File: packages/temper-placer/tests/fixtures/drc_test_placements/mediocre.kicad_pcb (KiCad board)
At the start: 2 copper layers, 50 x 30 mm, 4 parts, among them U1 LM358

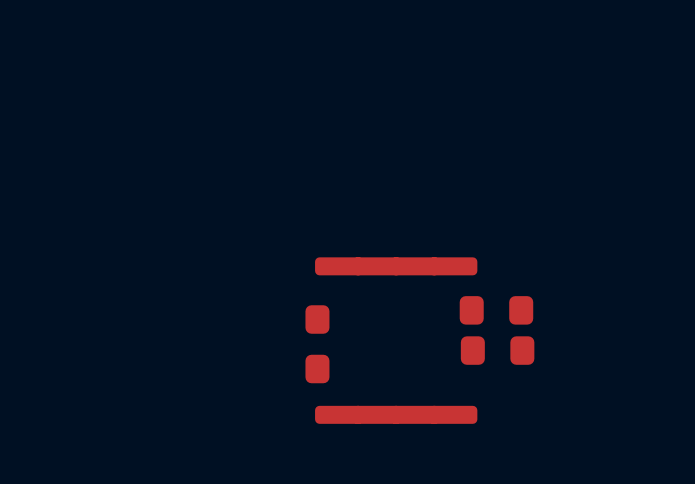
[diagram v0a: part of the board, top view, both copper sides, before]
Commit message: feat(placer): NSGA-II, Crawler, NetCentroidLoss, and structural refinements
- Implemented NSGA-II multi-objective optimization
- Added PcbCrawler for GitHub data collection
- Implemented NetCentroidAttractionLoss
- Unified optimization pipeline with explicit phases
- Fixed ruff linting errors and optimized imports
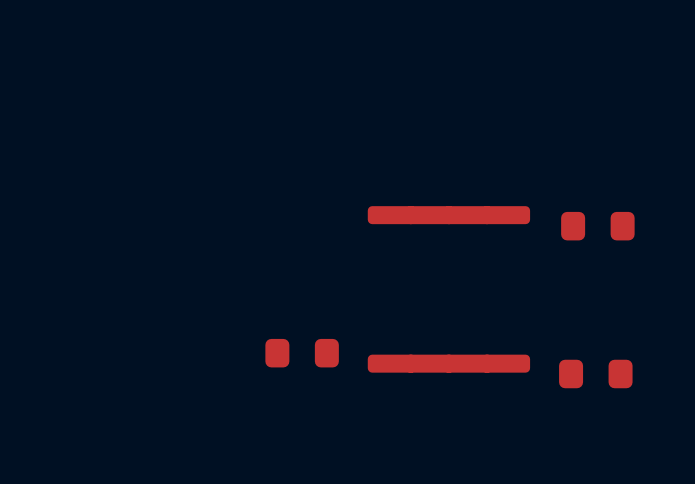
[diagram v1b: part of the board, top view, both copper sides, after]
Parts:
- moved C1 4.39 mm to (209.1, 149.6), turned to 180 degrees
- moved R2 3.37 mm to (209.0, 154.5)
- moved U1 2.45 mm to (204.1, 151.7)
- moved R1 0.59 mm to (199.2, 153.8), turned to 180 degrees
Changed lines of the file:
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@@
   (net 4 "SIG2")
   (footprint "Resistor_SMD:R_0603_1608Metric" (layer "F.Cu")
-    (at 199.748772873673 153.51630763178667 90.0)
+    (at 199.2375696681596 153.81366396913302 180.0)
     (property "Reference" "R1")
     (property "Value" "10k")
@@
   )
   (footprint "Resistor_SMD:R_0603_1608Metric" (layer "F.Cu")
-    (at 205.7534685396509 153.72662510139173 0.0)
+    (at 209.0270611652515 154.5077808807559 0.0)
     (property "Reference" "R2")
     (property "Value" "4.7k")
@@
   )
   (footprint "Capacitor_SMD:C_0603_1608Metric" (layer "F.Cu")
-    (at 205.71572434426218 152.38670351602337 0.0)
+    (at 209.0957264059502 149.57992738646345 180.0)
     (property "Reference" "C1")
     (property "Value" "100nF")
@@
   )
   (footprint "Package_SO:SOIC-8_3.9x4.9mm_P1.27mm" (layer "F.Cu")
-    (at 202.37346147158888 153.3943308817871 90.0)
+    (at 204.1311600303306 151.6876553482217 90.0)
     (property "Reference" "U1")
     (property "Value" "LM358")

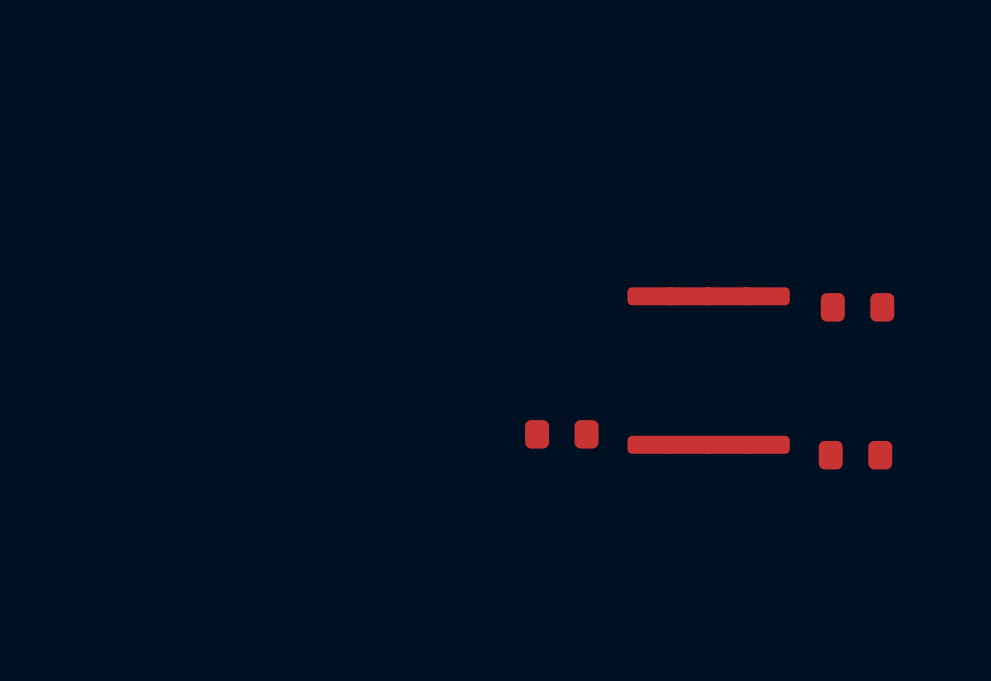
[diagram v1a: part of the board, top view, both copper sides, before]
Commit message: feat(placer): vectorize GroundCrossingLoss and add star-ground awareness
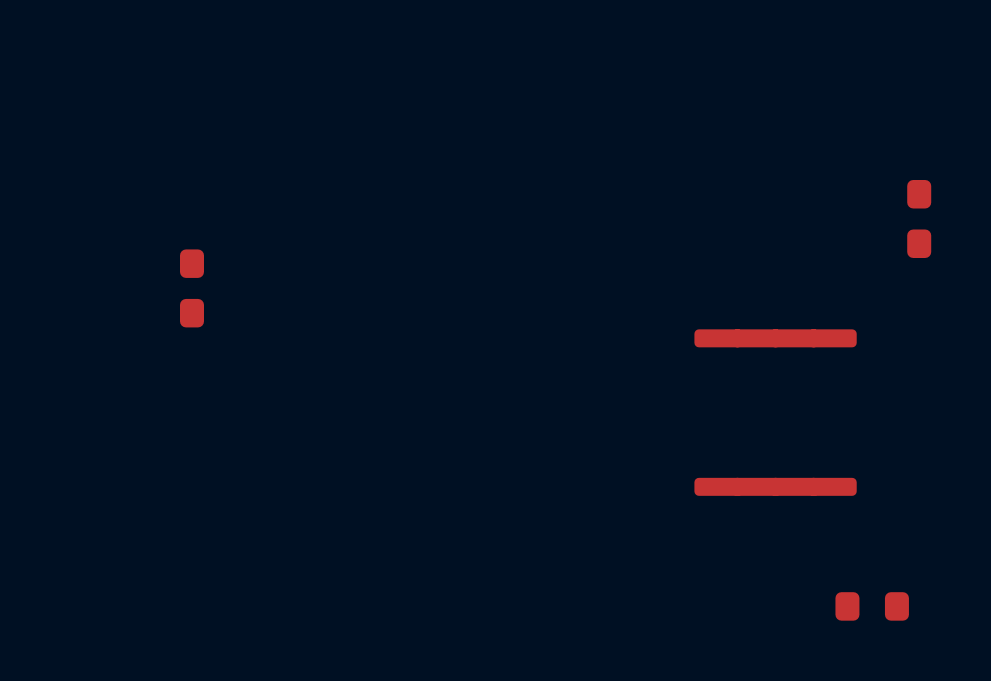
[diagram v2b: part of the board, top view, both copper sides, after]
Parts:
- moved R1 13.3 mm to (186.9, 148.9), turned to 90 degrees
- moved R2 5.07 mm to (209.6, 159.5), turned to 180 degrees
- moved C1 3.59 mm to (211.2, 146.6), turned to 270 degrees
- moved U1 2.63 mm to (206.4, 153.1)
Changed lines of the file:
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@@
   (net 4 "SIG2")
   (footprint "Resistor_SMD:R_0603_1608Metric" (layer "F.Cu")
-    (at 199.2375696681596 153.81366396913302 180.0)
+    (at 186.91073359716347 148.9497742597683 90.0)
     (property "Reference" "R1")
     (property "Value" "10k")
@@
   )
   (footprint "Resistor_SMD:R_0603_1608Metric" (layer "F.Cu")
-    (at 209.0270611652515 154.5077808807559 0.0)
+    (at 209.58405890750464 159.54938949343563 180.0)
     (property "Reference" "R2")
     (property "Value" "4.7k")
@@
   )
   (footprint "Capacitor_SMD:C_0603_1608Metric" (layer "F.Cu")
-    (at 209.0957264059502 149.57992738646345 180.0)
+    (at 211.1511315029556 146.63530564857916 270.0)
     (property "Reference" "C1")
     (property "Value" "100nF")
@@
   )
   (footprint "Package_SO:SOIC-8_3.9x4.9mm_P1.27mm" (layer "F.Cu")
-    (at 204.1311600303306 151.6876553482217 90.0)
+    (at 206.36288493972353 153.08851482101375 90.0)
     (property "Reference" "U1")
     (property "Value" "LM358")

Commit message: feat: Consolidate implementations for Manufacturing, Star Point, and Analysis tasks
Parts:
- turned C1 to 90 degrees
- turned R1 to 270 degrees
- turned R2 to 270 degrees
- turned U1 to 270 degrees
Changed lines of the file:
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@@
   (net 4 "SIG2")
   (footprint "Resistor_SMD:R_0603_1608Metric" (layer "F.Cu")
-    (at 186.91073359716347 148.9497742597683 90.0)
+    (at 186.91073359716347 148.9497742597683 270.0)
     (property "Reference" "R1")
     (property "Value" "10k")
@@
   )
   (footprint "Resistor_SMD:R_0603_1608Metric" (layer "F.Cu")
-    (at 209.58405890750464 159.54938949343563 180.0)
+    (at 209.58405890750464 159.54938949343563 270.0)
     (property "Reference" "R2")
     (property "Value" "4.7k")
@@
   )
   (footprint "Capacitor_SMD:C_0603_1608Metric" (layer "F.Cu")
-    (at 211.1511315029556 146.63530564857916 270.0)
+    (at 211.1511315029556 146.63530564857916 90.0)
     (property "Reference" "C1")
     (property "Value" "100nF")
@@
   )
   (footprint "Package_SO:SOIC-8_3.9x4.9mm_P1.27mm" (layer "F.Cu")
-    (at 206.36288493972353 153.08851482101375 90.0)
+    (at 206.36288493972353 153.08851482101375 270.0)
     (property "Reference" "U1")
     (property "Value" "LM358")

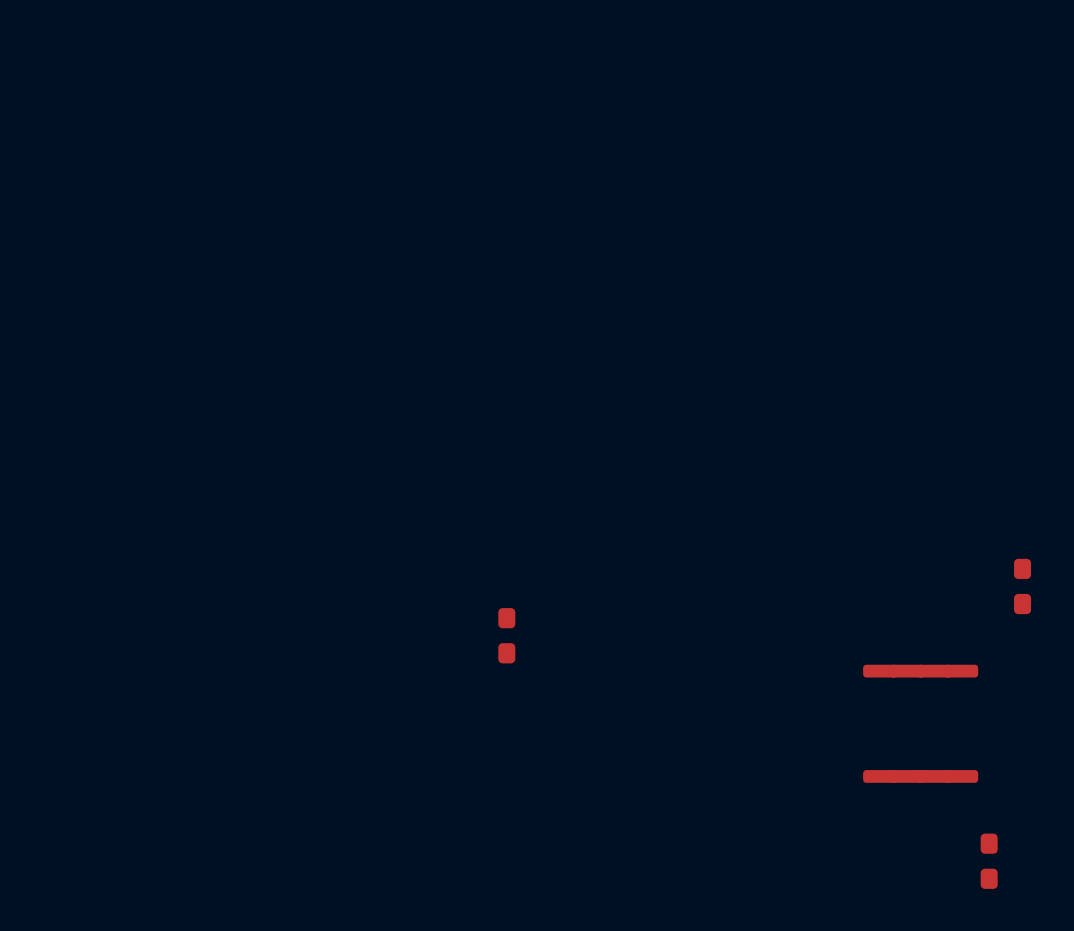
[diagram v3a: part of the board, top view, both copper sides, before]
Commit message: fix(placer): resolve all critical optimizer bugs in temper-p11g
- Fixed JAX array len() TypeErrors by using .shape[0]\n- Corrected BoundaryLoss to use absolute coordinates for non-zero origin boards\n- Implemented hard position and virtual node clamping in training loop\n- Fixed TypeError in force_directed.py random_init call\n- Cleaned up outdated Board/Component signatures in tests
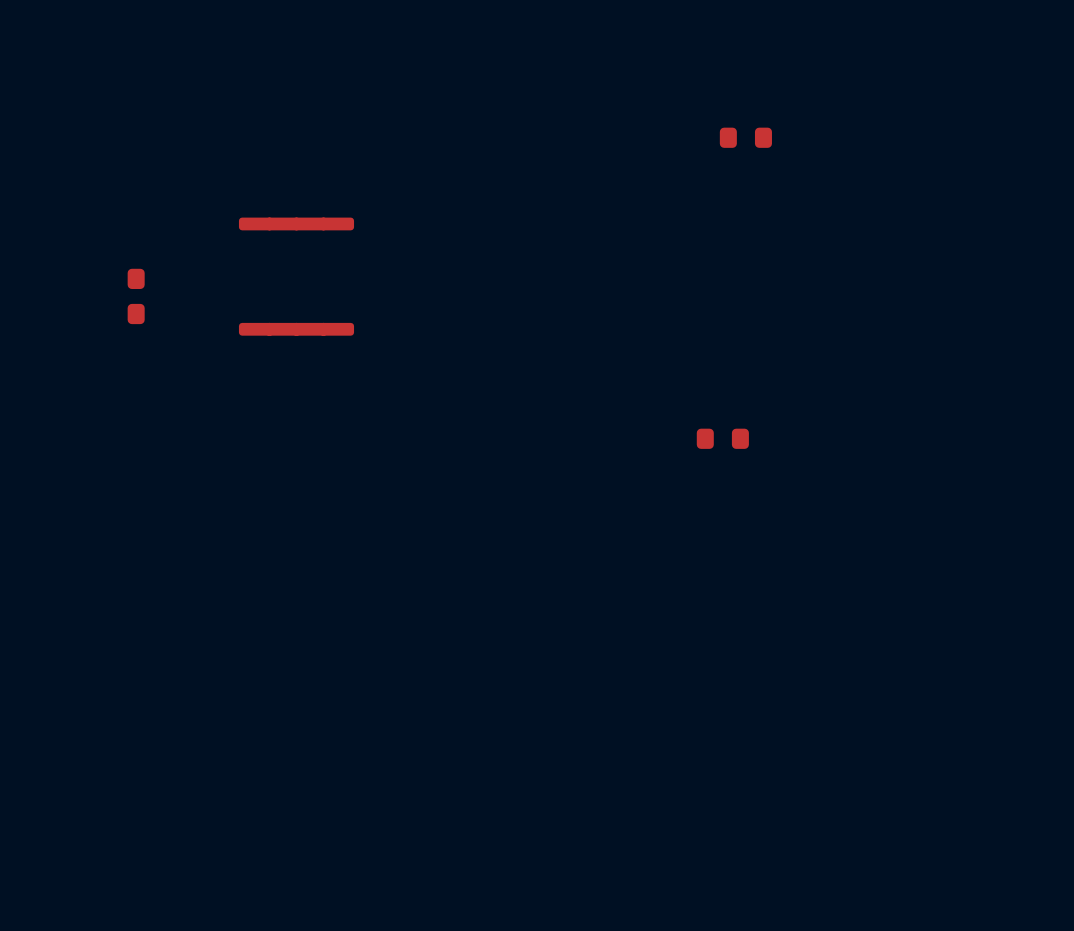
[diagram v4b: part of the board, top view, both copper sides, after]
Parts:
- moved U1 36.1 mm to (177.0, 132.1), turned to 90 degrees
- moved C1 24.8 mm to (198.1, 125.5), turned to 0 degrees
- moved R1 23.6 mm to (169.5, 133.0), turned to 90 degrees
- moved R2 23.5 mm to (197.1, 139.7), turned to 180 degrees
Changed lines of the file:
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@@
   (net 4 "SIG2")
   (footprint "Resistor_SMD:R_0603_1608Metric" (layer "F.Cu")
-    (at 186.91073359716347 148.9497742597683 270.0)
+    (at 169.4893702821547 133.00261733309864 90.0)
     (property "Reference" "R1")
     (property "Value" "10k")
@@
   )
   (footprint "Resistor_SMD:R_0603_1608Metric" (layer "F.Cu")
-    (at 209.58405890750464 159.54938949343563 270.0)
+    (at 197.06575616552115 139.69270442474038 180.0)
     (property "Reference" "R2")
     (property "Value" "4.7k")
@@
   )
   (footprint "Capacitor_SMD:C_0603_1608Metric" (layer "F.Cu")
-    (at 211.1511315029556 146.63530564857916 90.0)
+    (at 198.1497315978143 125.54342349336588 0.0)
     (property "Reference" "C1")
     (property "Value" "100nF")
@@
   )
   (footprint "Package_SO:SOIC-8_3.9x4.9mm_P1.27mm" (layer "F.Cu")
-    (at 206.36288493972353 153.08851482101375 270.0)
+    (at 177.02590206250323 132.07108369440687 90.0)
     (property "Reference" "U1")
     (property "Value" "LM358")
